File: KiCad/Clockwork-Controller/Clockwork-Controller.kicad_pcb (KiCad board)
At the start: 2 copper layers, 56.4 x 94.2 mm, 97 parts, among them CN2 PJ-307N5, J2 to DIN-6 Male, J3 Pause Button, J4 ICSP, J5 LED-Connector, Q1 AO3400A, Q2 SS8050, Q3 SS8050, Q4 SS8050, SW1 Guide/Follow, SW2 Mode -, SW3 Mode +, SW4 Frame -, SW5 Frame +, U1 ECS-TXO-3225MV-160-TR, U2 AP2210N-3.3TRG1, U3 74HCT14, U4 G3VM-61VY3(TR), U5 MCP4725, U6 LMC6482, U7 ATmega328P-A

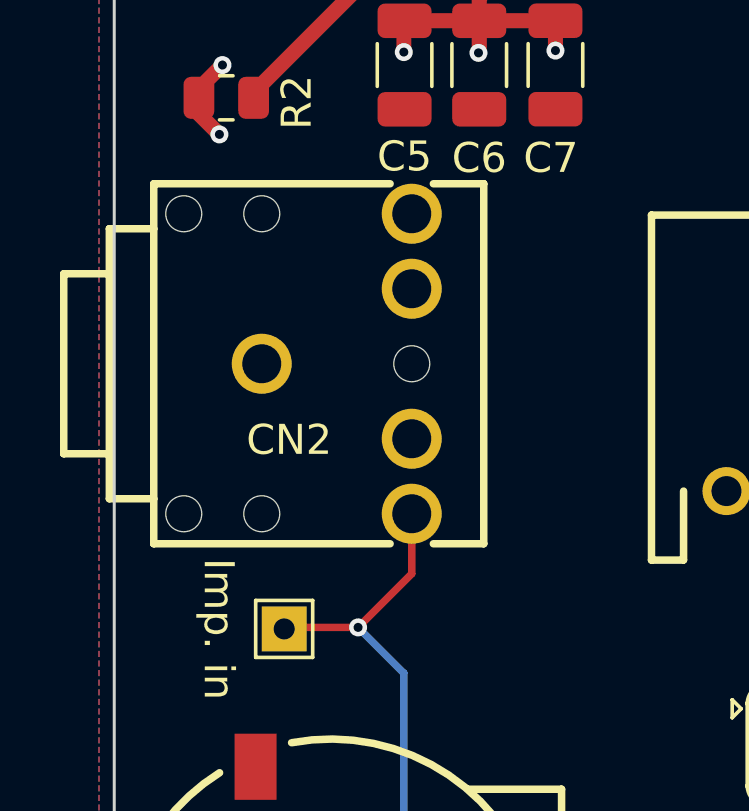
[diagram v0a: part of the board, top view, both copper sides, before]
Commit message: Moving the 3.5mm jack inwards to be flush with the edge
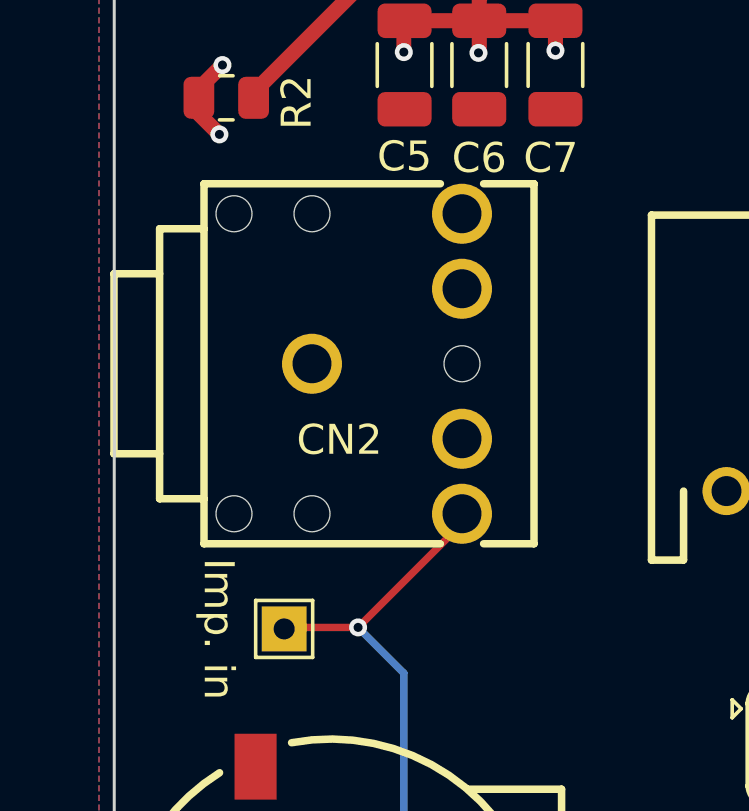
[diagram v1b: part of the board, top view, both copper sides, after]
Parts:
- moved CN2 1.68 mm to (47.7, 39.4)
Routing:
- net Net-(CN2-Pad2): track 30.7 -> 31.4 mm
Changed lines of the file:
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@@
 			)
 		)
-		(property "LCSC Part" "C93156"
+		(property "LCSC Part" ""
 			(at 0 0 0)
 			(unlocked yes)
@@
 	(footprint "easyEDA:AUDIO-TH_PJ-307N5"
 		(layer "F.Cu")
-		(at 46.0248 39.37)
+		(at 47.7 39.37)
 		(property "Reference" "CN2"
 			(at -1.5856 2.54 0)
@@
 			)
 		)
-		(property "LCSC Part" "C93156"
+		(property "LCSC Part" ""
 			(at 0 0 0)
 			(unlocked yes)
@@
 			)
 		)
-		(property "LCSC Part" "C93156"
+		(property "LCSC Part" ""
 			(at 0 0 90)
 			(unlocked yes)
@@
 			)
 		)
-		(property "LCSC Part" "C93156"
+		(property "LCSC Part" ""
 			(at 0 0 0)
 			(unlocked yes)
@@
 	)
 	(segment
-		(start 48.5248 46.3696)
-		(end 48.5248 44.37)
+		(start 44.5008 48.1584)
+		(end 44.45 48.2092)
 		(width 0.25)
 		(layer "F.Cu")
@@
 	)
 	(segment
-		(start 44.5008 48.1584)
-		(end 44.45 48.2092)
+		(start 46.736 48.1584)
+		(end 44.5008 48.1584)
 		(width 0.25)
 		(layer "F.Cu")
@@
 	(segment
 		(start 46.736 48.1584)
-		(end 44.5008 48.1584)
+		(end 50.2 44.6944)
 		(width 0.25)
 		(layer "F.Cu")
@@
 	)
 	(segment
-		(start 46.736 48.1584)
-		(end 48.5248 46.3696)
+		(start 44.45 48.2092)
+		(end 44.2722 48.2092)
 		(width 0.25)
 		(layer "F.Cu")
@@
 	)
 	(segment
-		(start 44.45 48.2092)
-		(end 44.2722 48.2092)
+		(start 50.2 44.6944)
+		(end 50.2 44.37)
 		(width 0.25)
 		(layer "F.Cu")
